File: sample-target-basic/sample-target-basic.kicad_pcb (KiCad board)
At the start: 2 copper layers, 43 x 20 mm, 45 parts, among them J1 USB_C_Receptacle, J2 Conn_01x03, SW1 SW_Push, SW2 SW_Push, U1 MIC5504-3.3YM5, U2 W25Q128JVS, U3 RP2040, Y1 ABM8-272-T3

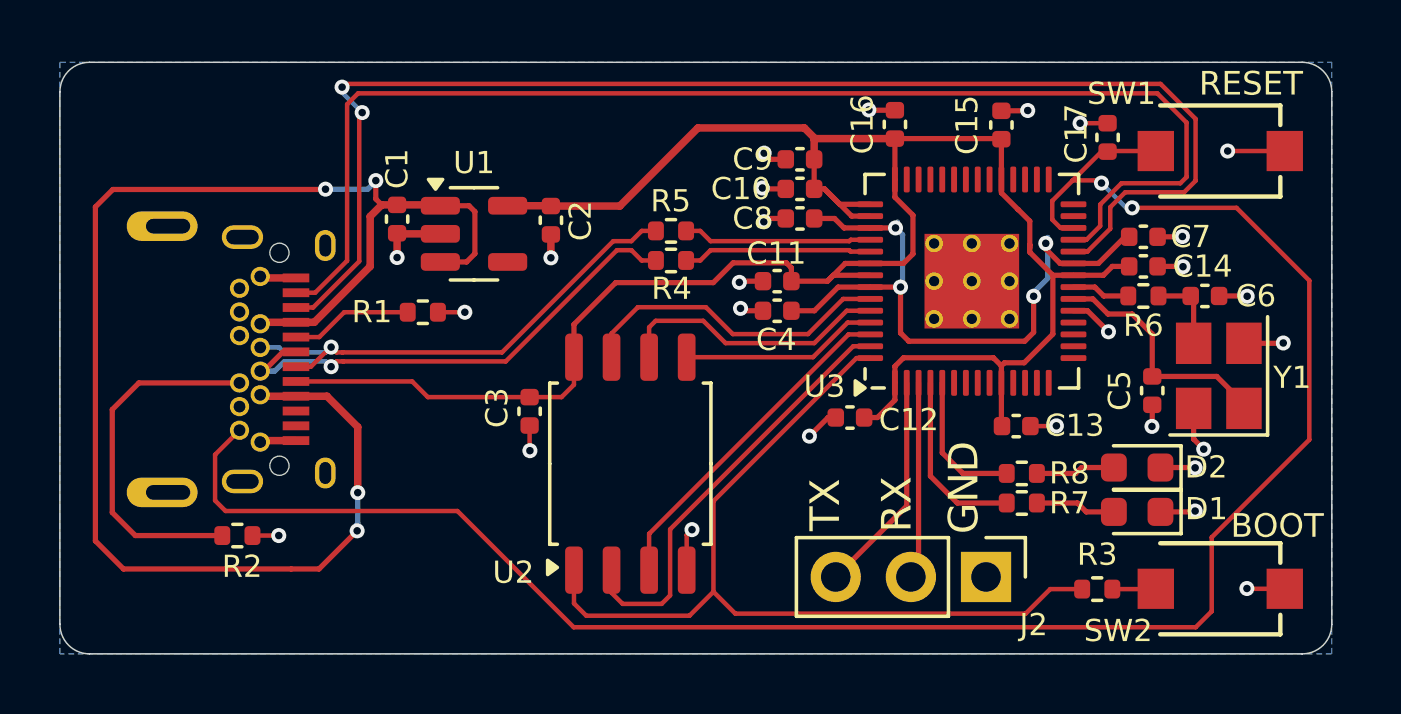
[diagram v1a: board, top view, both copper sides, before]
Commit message: Add CC lines to sample targets
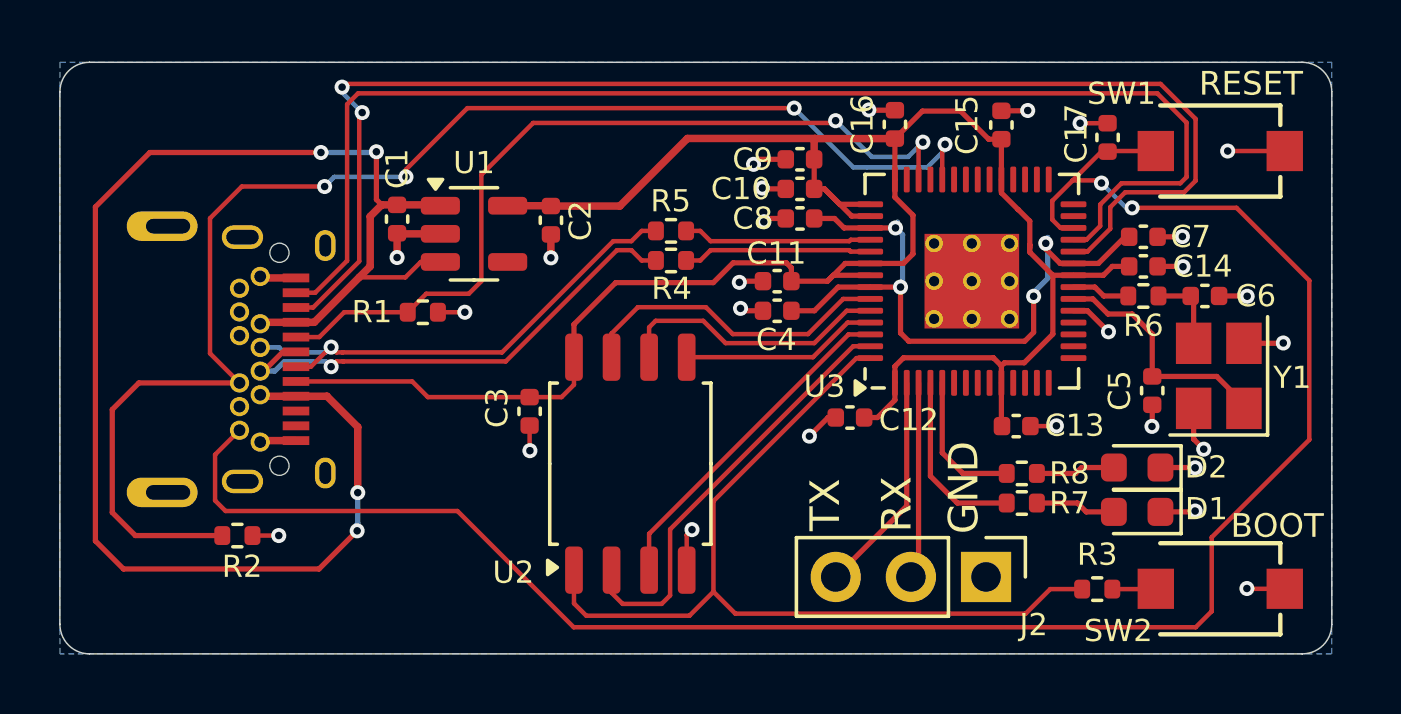
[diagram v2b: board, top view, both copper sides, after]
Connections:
- U3 pad 38: unconnected-(U3-GPIO26_ADC0-Pad38) -> /CC2
- U3 pad 40: unconnected-(U3-GPIO28_ADC2-Pad40) -> /CC1
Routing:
- net /CC2: track 12.2 -> 47.2 mm, vias 0 -> 4
- net /CC1: track 4.13 -> 28.4 mm, vias 0 -> 2

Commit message: Add pull up resistor to spi flash
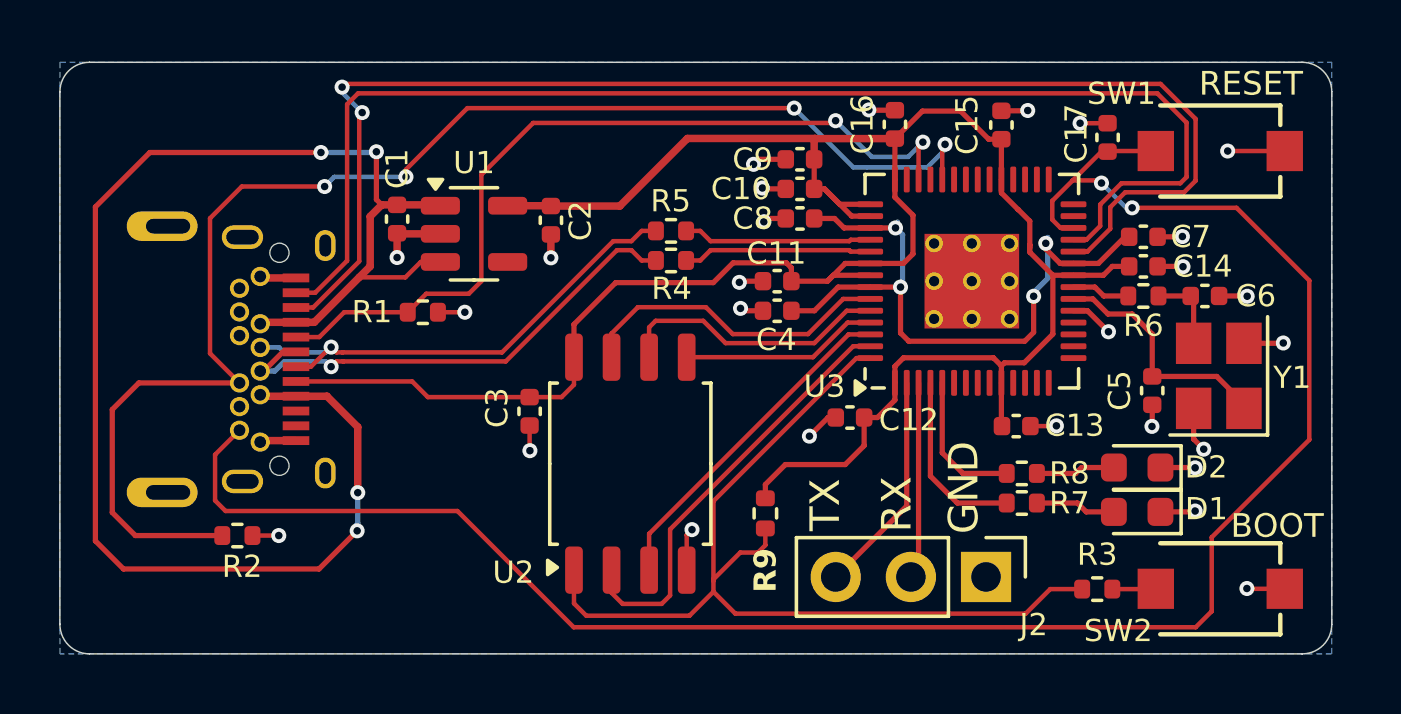
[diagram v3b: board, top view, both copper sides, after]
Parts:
- added R9: 1k, Resistor_SMD:R_0402_1005Metric, F.Cu at (100.8, 105.2)
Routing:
- net +3V3: track 75.5 -> 80.8 mm
- net /QSPI_SS: track 29.8 -> 32.7 mm
